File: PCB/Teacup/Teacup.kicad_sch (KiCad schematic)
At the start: 1 part

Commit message: pcb: pow + clock + usb
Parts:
- added C? (x2): TBD, Capacitor_SMD:C_0402_1005Metric, symbol Device:C
- added D?: D_TVS_Dual_AAC, symbol Device:D_TVS_Dual_AAC
- added J?: USB_C_Receptacle_USB2.0, symbol Connector:USB_C_Receptacle_USB2.0
- added R0, R1: 100k, Resistor_SMD:R_0603_1608Metric_Pad0.98x0.95mm_HandSolder, symbol Device:R
- added R? (x2): 5k1, Resistor_SMD:R_0603_1608Metric_Pad0.98x0.95mm_HandSolder, symbol Device:R
- added Y?: 24 MHz, Crystal:Crystal_SMD_2016-4Pin_2.0x1.6mm, symbol Device:Crystal_GND24
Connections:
- net +0V8: now also 1.10 (VDD_1), 1.30 (MIPI_AVD08), 1.39 (VDD_2), 1.55 (VDD_3), 1.72 (VDD_4), 1.78 (DDRPLL_VCCD), 1.83 (VDD_5)
- net +1V8: now also 1.3 (VDDIO_OSC), 1.31 (MIPI_AVD18), 1.33 (ADC_VREF), 1.34 (ADC_AVDD), 1.38 (USB_AVD18), 1.43 (CODEC_AVDD), 1.6 (PLL_VDDHV), 1.75 (DDRVDD), 1.76 (VDDMEM), 1.77 (VREF), 1.79 (DDRPLL_VCCA), 1.9 (VDDIO0)
- net +3V3: now also 1.37 (USB_AVD33), 1.40 (VDDIO2), 1.56 (VDDIO1_1), 1.84 (VDDIO1_2), R1.1
- net +5V: now also J?.A4 (VBUS), J?.A9 (VBUS), J?.B4 (VBUS), J?.B9 (VBUS)
- net GND: now also 1.8 (EFUSE_AVD), 1.89 (EP), C?.1, C?.2, D?.3 (common), J?.A1 (GND), J?.A12 (GND), J?.B1 (GND), J?.B12 (GND), R0.1, R?.1, R?.1, Y?.2, Y?.4
- net USB_D-: now reaches 1.35 (USB0PN)
- net USB_D-: now also D?.1 (A1), J?.A7 (D-), J?.B7 (D-)
- net USB_D+: now reaches 1.36 (USB0PP)
- net USB_D+: now also D?.2 (A2), J?.A6 (D+), J?.B6 (D+)
- net at 1.4 (EXCLK_O): now also C?.1, Y?.3
- net at 1.5 (EXCLK_I): now also C?.2, Y?.1
- net at 1.67 (BOOT_SEL0_PC00): now also R0.2, R1.2
- new net: J?.A5 (CC1), R?.2
- new net: J?.B5 (CC2), R?.2
- no-connect marks 0 -> 4
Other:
- note added: "Boot Selection R1 - NOR - MMC - USB R0 - MMC - USB"
- note added: "General purpose I/O: 1.5~3.6V DDR I/O: 1.8V(DDR2) ± 0.1V EFUSE programming: 1.8V ± 10% Analog power supply 1: 1.8V ± 10% Analog power supply 2: 3.3V ± 10% Core: 0.8V ± 0.1V 9 VDDIO0: IO digital power for DVP power domain, 1.8V 56,84 VDDIO1: IO digital power for normal function Pad power domain,1.8V/3.3V 40 VDDIO2: IO digital power for normal function Pad power domain, 1.8V/3.3V 10,39,55,72,83 VDD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"

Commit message: pcb: regulators
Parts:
- added C? (x6): 10uF, Capacitor_SMD:C_0402_1005Metric, symbol Device:C
- added C? (x6): 100nF, Capacitor_SMD:C_0402_1005Metric, symbol Device:C
- added C? (x6): 1uF, Capacitor_SMD:C_0402_1005Metric, symbol Device:C
- added R? (x6): 0R, Resistor_SMD:R_0603_1608Metric_Pad0.98x0.95mm_HandSolder, symbol Device:R
- added U?: AZ1117-1.8, symbol Regulator_Linear:AZ1117-1.8
- added U?: AZ1117-3.3, symbol Regulator_Linear:AZ1117-3.3
- added U?: MCP1826S, symbol Regulator_Linear:MCP1826S
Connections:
- net +0V8: now also R?.1
- net +1V8: now also R?.1
- net +3V3: now also R?.1, R?.1, R?.1
- net +5V: now also R?.1
- net GND: now also C?.2, C?.2, C?.2, C?.2, C?.2, C?.2, C?.2, C?.2, C?.2, C?.2, C?.2, C?.2, C?.2, C?.2, C?.2, C?.2, C?.2, C?.2, U?.1 (GND), U?.1 (GND), U?.2 (GND)
- new net: C?.1, C?.1, C?.1, R?.2, U?.3 (VI) (x2)
- new net: C?.1, C?.1, C?.1, R?.2, U?.2 (VO) (x2)
- new net: C?.1, C?.1, C?.1, R?.2, U?.1 (VI)
- new net: C?.1, C?.1, C?.1, R?.2, U?.3 (VO)
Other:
- moved on the sheet: 1, C?, D?, J?, R0, R1, R?, Y?

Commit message: pcb: flash + footprints
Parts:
- added C19, C23, C24: 100nF, Capacitor_SMD:C_0603_1608Metric_Pad1.08x0.95mm_HandSolder, symbol Device:C
- added C22: 4.7uF, Capacitor_SMD:C_0603_1608Metric_Pad1.08x0.95mm_HandSolder, symbol Device:C
- added J2: SD_Card, symbol Connector:SD_Card
- added R10, R11, R12, R13, R14: 100k, Resistor_SMD:R_0603_1608Metric_Pad0.98x0.95mm_HandSolder, symbol Device:R
- added R15, R16, R17, R18, R19, R20: 47k, Resistor_SMD:R_0603_1608Metric_Pad0.98x0.95mm_HandSolder, symbol Device:R
- added R21: 1M, Resistor_SMD:R_0402_1005Metric, symbol Device:R
- added U4: W25Q32JVSS, Package_SO:SOIC-8_5.23x5.23mm_P1.27mm, symbol Memory_Flash:W25Q32JVSS
- C1, C10, C11, C12, C13, C14, C15, C16, C17, C18, C2, C3, C4, C5, C6, C7, C8, C9: renamed from C?; footprint Capacitor_SMD:C_0402_1005Metric -> Capacitor_SMD:C_0603_1608Metric_Pad1.08x0.95mm_HandSolder
- D1: renamed from D?; footprint (none) -> Package_TO_SOT_SMD:SOT-323_SC-70
- IC1: renamed from 1; Reference_1 IC -> (none); Value_1 T31ZX -> (none)
- gave numbers to parts that had none: 15
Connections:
- net +1V8: now also R10.1; no longer IC1.77 (VREF)
- net +3V3: now also C23.1, C24.1, J2.4 (VDD), R12.2, R13.1, R14.2, R15.1, R16.1, R17.1, R18.1, R19.1, R20.1, U4.8 (VCC)
- net GND: now also C19.1, C22.2, C23.2, C24.2, J2.3 (VSS), J2.6 (VSS), R11.1, U4.4 (GND)
- net at C21.1, IC1.4 (EXCLK_O), Y1.3: now also R21.2
- net at IC1.42 (VCM): now also C22.1
- net NOR_CE: now reaches IC1.45 (SFC_CE0_PA28)
- net NOR_CE: now also R12.1, U4.1 (~{CS})
- net NOR_DR: now reaches IC1.46 (SFC_DR_PA24)
- net NOR_DR: now also U4.2 (DO(IO1))
- net NOR_DT: now reaches IC1.47 (SFC_DT_PA23)
- net NOR_DT: now also U4.5 (DI(IO0))
- net NOR_CK: now reaches IC1.48 (SFC_CLK_PA27)
- net NOR_CK: now also U4.6 (CLK)
- net MMC0_D1: now reaches IC1.49 (MSC0_D1_SSI_SLV_DR_PB01)
- net MMC0_D1: now also J2.8 (DAT1), R20.2
- net at C20.2, IC1.5 (EXCLK_I), Y1.1: now also R21.1
- net MMC0_D0: now reaches IC1.50 (MSC0_D0_SSI_SLV_DT_PB00)
- net MMC0_D0: now also J2.7 (DAT0), R19.2
- net MMC0_CLK: now reaches IC1.51 (MSC0_CLK_SSI_SLV_CLK_PB04)
- net MMC0_CLK: now also J2.5 (CLK), R18.2
- net MMC0_CMD: now reaches IC1.52 (MSC0_CMD_SSI_SLV_CE0_PB05)
- net MMC0_CMD: now also J2.2 (CMD), R17.2
- net MMC0_D3: now reaches IC1.53 (MSC0_D3_PB03)
- net MMC0_D3: now also J2.1 (CD/DAT3), R16.2
- net MMC0_D2: now reaches IC1.54 (MSC0_D2_PB02)
- net MMC0_D2: now also J2.9 (DAT2), R15.2
- new net: R13.2, U4.3 (IO2)
- new net: C19.2, IC1.77 (VREF), R10.2, R11.2
- new net: R14.1, U4.7 (IO3)
- no-connect marks 4 -> 8
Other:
- note added: "General purpose I/O: 1.5~3.6V DDR I/O: 1.8V(DDR2) ± 0.1V EFUSE programming: 1.8V ± 10% Analog power supply 1: 1.8V ± 10% Analog power supply 2: 3.3V ± 10% Core: 0.8V ± 0.1V"
- note removed: "General purpose I/O: 1.5~3.6V DDR I/O: 1.8V(DDR2) ± 0.1V EFUSE programming: 1.8V ± 10% Analog power supply 1: 1.8V ± 10% Analog power supply 2: 3.3V ± 10% Core: 0.8V ± 0.1V 9 VDDIO0: IO digital power for DVP power domain, 1.8V 56,84 VDDIO1: IO digital power for normal function Pad power domain,1.8V/3.3V 40 VDDIO2: IO digital power for normal function Pad power domain, 1.8V/3.3V 10,39,55,72,83 VDD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"
- moved on the sheet: C20, C21, Y1

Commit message: pcb: sch done, initial placement
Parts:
- added J3: SFW15R-2STE1LF, Footprints:SFW15R2STE1LF, symbol SFW15R-2STE1LF:SFW15R-2STE1LF
- added J4: EXP0, Connector_PinHeader_2.54mm:PinHeader_1x10_P2.54mm_Vertical, symbol Connector:Conn_01x10_Female
- added J5: UART, Connector_PinHeader_2.54mm:PinHeader_1x03_P2.54mm_Vertical, symbol Connector:Conn_01x03_Female
- added J6: EXP2, Connector_PinHeader_2.54mm:PinHeader_1x16_P2.54mm_Vertical, symbol Connector:Conn_01x16_Female
- added J7: EXP1, Connector_PinHeader_2.54mm:PinHeader_1x16_P2.54mm_Vertical, symbol Connector:Conn_01x16_Female
- J1: footprint (none) -> Connector_USB:USB_C_Receptacle_HRO_TYPE-C-31-M-12
- J2: footprint (none) -> Connector_Card:SD_Hirose_DM1AA_SF_PEJ82
- U1, U2, U3: footprint (none) -> Kicad:SOT-223-3_TabPin2
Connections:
- net +3V3: now also J3.15, J6.15 (Pin_15), J6.16 (Pin_16)
- net GND: now also J3.1, J3.10, J3.4, J3.7, J5.3 (Pin_3), J6.1 (Pin_1), J6.11 (Pin_11), J6.14 (Pin_14), J6.5 (Pin_5), J6.8 (Pin_8)
- net at IC1.1 (PWM0_SSI1_DT_PB17): now also J7.15 (Pin_15)
- net CAM_PE: now reaches IC1.11 (SA2_PA18)
- net CAM_PE: now also J3.11
- net I2C0_SCK: now reaches IC1.12 (SD7_SMB0_SCK_PA13)
- net I2C0_SCK: now also J3.13
- net I2C0_SDA: now reaches IC1.13 (SD6_SMB0_SDA_PA12)
- net I2C0_SDA: now also J3.14
- net PA17: now reaches IC1.14 (RD_DVP_VSYNC_SMB1_SCK_MSC1_CMD_PA17)
- net PA17: now also J4.10 (Pin_10)
- net PA16: now reaches IC1.15 (CS2_DVP_HSYNC_SMB1_SDA_MSC1_CLK_PA16)
- net PA16: now also J4.9 (Pin_9)
- net PA15: now reaches IC1.16 (SA1_DVP_MCLK_PA15)
- net PA15: now also J4.8 (Pin_8)
- net PA14: now reaches IC1.17 (SA0_DVP_PCLK_PWM0_PA14)
- net PA14: now also J4.7 (Pin_7)
- net PA11: now reaches IC1.18 (SD5_DVP_D11_UART2_RXD_MSC1_D3_PA11)
- net PA11: now also J4.6 (Pin_6)
- net PA10: now reaches IC1.19 (SD4_DVP_D10_UART2_TXD_MSC1_D2_PA10)
- net PA10: now also J4.5 (Pin_5)
- net at IC1.2 (PWM1_SSI1_DR_PB18): now also J7.16 (Pin_16)
- net PA09: now reaches IC1.20 (SD3_DVP_D9_UART2_RTS_MSC1_D1_PA09)
- net PA09: now also J4.4 (Pin_4)
- net PA08: now reaches IC1.21 (SD2_DVP_D8_UART2_CTS_MSC1_D0_PA08)
- net PA08: now also J4.3 (Pin_3)
- net PA07: now reaches IC1.22 (SD1_DVP_D7_UART1_RXD_PA07)
- net PA07: now also J4.2 (Pin_2)
- net PA06: now reaches IC1.23 (SD0_DVP6_UART1_TXD_PA06)
- net PA06: now also J4.1 (Pin_1)
- net MIPI_0_N: now reaches IC1.24 (MIPI_DATAN0_DVP_D5)
- net MIPI_0_N: now also J3.2
- net MIPI_0_P: now reaches IC1.25 (MIPI_DATAP0_DVP_D4)
- net MIPI_0_P: now also J3.3
- net MIPI_CLK_N: now reaches IC1.26 (MIPI_CLKN_DVP_D3)
- net MIPI_CLK_N: now also J3.8
- net MIPI_CLK_P: now reaches IC1.27 (MIPI_CLKP_DVP_D2)
- net MIPI_CLK_P: now also J3.9
- net MIPI_1_N: now reaches IC1.28 (MIPI_DATAN1_DVP_D1)
- net MIPI_1_N: now also J3.5
- net MIPI_1_P: now reaches IC1.29 (MIPI_DATAP1_DVP_D0)
- net MIPI_1_P: now also J3.6
- net AUX0: now reaches IC1.32 (ADC_AUX0)
- net AUX0: now also J6.2 (Pin_2)
- net MICLP: now reaches IC1.41 (MICLP)
- net MICLP: now also J6.3 (Pin_3)
- net HPOUTL: now reaches IC1.44 (HPOUTL)
- net HPOUTL: now also J6.4 (Pin_4)
- net at IC1.57 (GMAC_MDIO_MSC1_D1_SLCD_D5_PB11): now also J7.1 (Pin_1)
- net at IC1.58 (GMAC_MDCK_MSC1_D0_I2S_SDTO_SLCD_D4_PB10): now also J7.2 (Pin_2)
- net at IC1.59 (GMAC_RXDV_MSC1_CMD_I2S_SDTI_SLCD_D3_PB09): now also J7.3 (Pin_3)
- net at IC1.60 (GMAC_RXD0_I2S_DAC_LRCK_SLCD_WR_PB15/_SFC_CE1_PA26): now also J7.4 (Pin_4)
- net at IC1.61 (GMAC_RXD1_SLCD_TE_PB16/_SFC_GPC_PA25): now also J7.5 (Pin_5)
- net at IC1.62 (GMAC_TXCLK_SLCD_D0_PB06): now also J7.6 (Pin_6)
- net at IC1.63 (GMAC_PHY_CLK_SLCD_D1_PB07): now also J7.7 (Pin_7)
- net at IC1.64 (GMAC_TXD0_MSC1_D2_I2S_ADC_LRCK_SLCD_D6_PB13): now also J7.8 (Pin_8)
- net at IC1.65 (GMAC_TXD1_MSC1_D3_I2S_DAC_MCLK_SLCD_D7_PB14): now also J7.9 (Pin_9)
- net at IC1.66 (GMAC_TXEN_MSC1_CLK_I2S_ADC_MCLK_SLCD_D2_PB08): now also J7.10 (Pin_10)
- net at IC1.68 (UART0_RTS_I2S_DAC_BCLK_SLCD_DC_PB21): now also J7.11 (Pin_11)
- net at IC1.69 (UART0_CTS_I2S_ADC_BCLK_SLCD_CS_PB20): now also J7.12 (Pin_12)
- net at IC1.70 (UART0_TXD_TDO_SLCD_RDY_PB22): now also J7.13 (Pin_13)
- net at IC1.71 (UART0_RXD_TDI_PB19): now also J7.14 (Pin_14)
- net UART_RX: now reaches IC1.73 (UART1_RXD_TMS_PB24)
- net UART_RX: now also J5.2 (Pin_2)
- net UART_TX: now reaches IC1.74 (UART1_TXD_TCK_PB23)
- net UART_TX: now also J5.1 (Pin_1)
- net CAM_LED: now reaches IC1.80 (GPIO_PB31)
- net CAM_LED: now also J3.12
- net PB30: now reaches IC1.81 (SSI1_CE0_DMIC_DAT1_PB30)
- net PB30: now also J6.13 (Pin_13)
- net PB29: now reaches IC1.82 (SSI1_CLK_DMIC_DAT0_PB29)
- net PB29: now also J6.12 (Pin_12)
- net PB28: now reaches IC1.85 (PWM3_SSI1_DR_DMIC_CLK_PB28)
- net PB28: now also J6.10 (Pin_10)
- net PB27: now reaches IC1.86 (PWM2_SSI1_DT_DRV_VBUS_PB27)
- net PB27: now also J6.9 (Pin_9)
- net PB26: now reaches IC1.87 (SMB1_SCK_SSI1_CLK_PB26)
- net PB26: now also J6.7 (Pin_7)
- net PB25: now reaches IC1.88 (SMB1_SDA_SSI1_CE0_PB25)
- net PB25: now also J6.6 (Pin_6)
- no-connect marks 8 -> 10

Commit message: pcb: routed high speed signals
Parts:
- added C25, C26, C28, C30, C31, C32, C34, C35, C36, C37, C38, C39, C40, C41, C42, C43, C44, C45, C46: 100nF, Capacitor_SMD:C_0402_1005Metric, symbol Device:C
- added TP1, TP2, TP3, TP4, TP5, TP6, TP7, TP8, TP9: TestPoint, TestPoint:TestPoint_Pad_D1.5mm, symbol Connector:TestPoint
- added U5: W25Q32JVSS, Package_DIP:DIP-8_W7.62mm_Socket_LongPads, symbol Memory_Flash:W25Q32JVSS
- C23, C24: footprint Capacitor_SMD:C_0603_1608Metric_Pad1.08x0.95mm_HandSolder -> Capacitor_SMD:C_0402_1005Metric
- J1: value USB_C_Receptacle_USB2.0 -> USB Type-C; Manufacturer (none) -> Korean Hroparts Elec; Manufacturer Part Number (none) -> TYPE-C-31-M-12
- J4, J5, J6, J7: now left out of the parts list
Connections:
- net +0V8: now also C37.1, C41.1, C42.1, C43.1, C44.1, C45.1, C46.1
- net +1V8: now also C25.1, C26.1, C28.1, C30.1, C31.1, C32.1, C34.1, C35.1
- net +3V3: now also C36.1, C38.1, C39.1, C40.1, U5.8 (VCC)
- net GND: now also C25.2, C26.2, C28.2, C30.2, C31.2, C32.2, C34.2, C35.2, C36.2, C37.2, C38.2, C39.2, C40.2, C41.2, C42.2, C43.2, C44.2, C45.2, C46.2, TP8.1, U5.4 (GND)
- net I2C0_SCK: now also TP9.1
- net I2C0_SDA: now also TP7.1
- net NOR_CE: now also U5.1 (~{CS})
- net NOR_CK: now also U5.6 (CLK)
- net NOR_DR: now also U5.2 (DO(IO1))
- net NOR_DT: now also U5.5 (DI(IO0))
- net USB_D+: now also TP5.1
- net USB_D-: now also TP3.1
- net at R13.2, U4.3 (IO2): now also U5.3 (IO2)
- net at C4.1, C5.1, C6.1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: now also TP2.1
- net at C16.1, C17.1, C18.1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: now also TP6.1
- net at C10.1, C11.1, C12.1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: now also TP4.1
- net at C1.1, C2.1, C3.1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: now also TP1.1
- net at R14.1, U4.7 (IO3): now also U5.7 (IO3)
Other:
- note added: "Flash Socket"
- moved on the sheet: C23, C24, J2, R12, R13, R14, R15, R16, R17, R18, R19, R20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

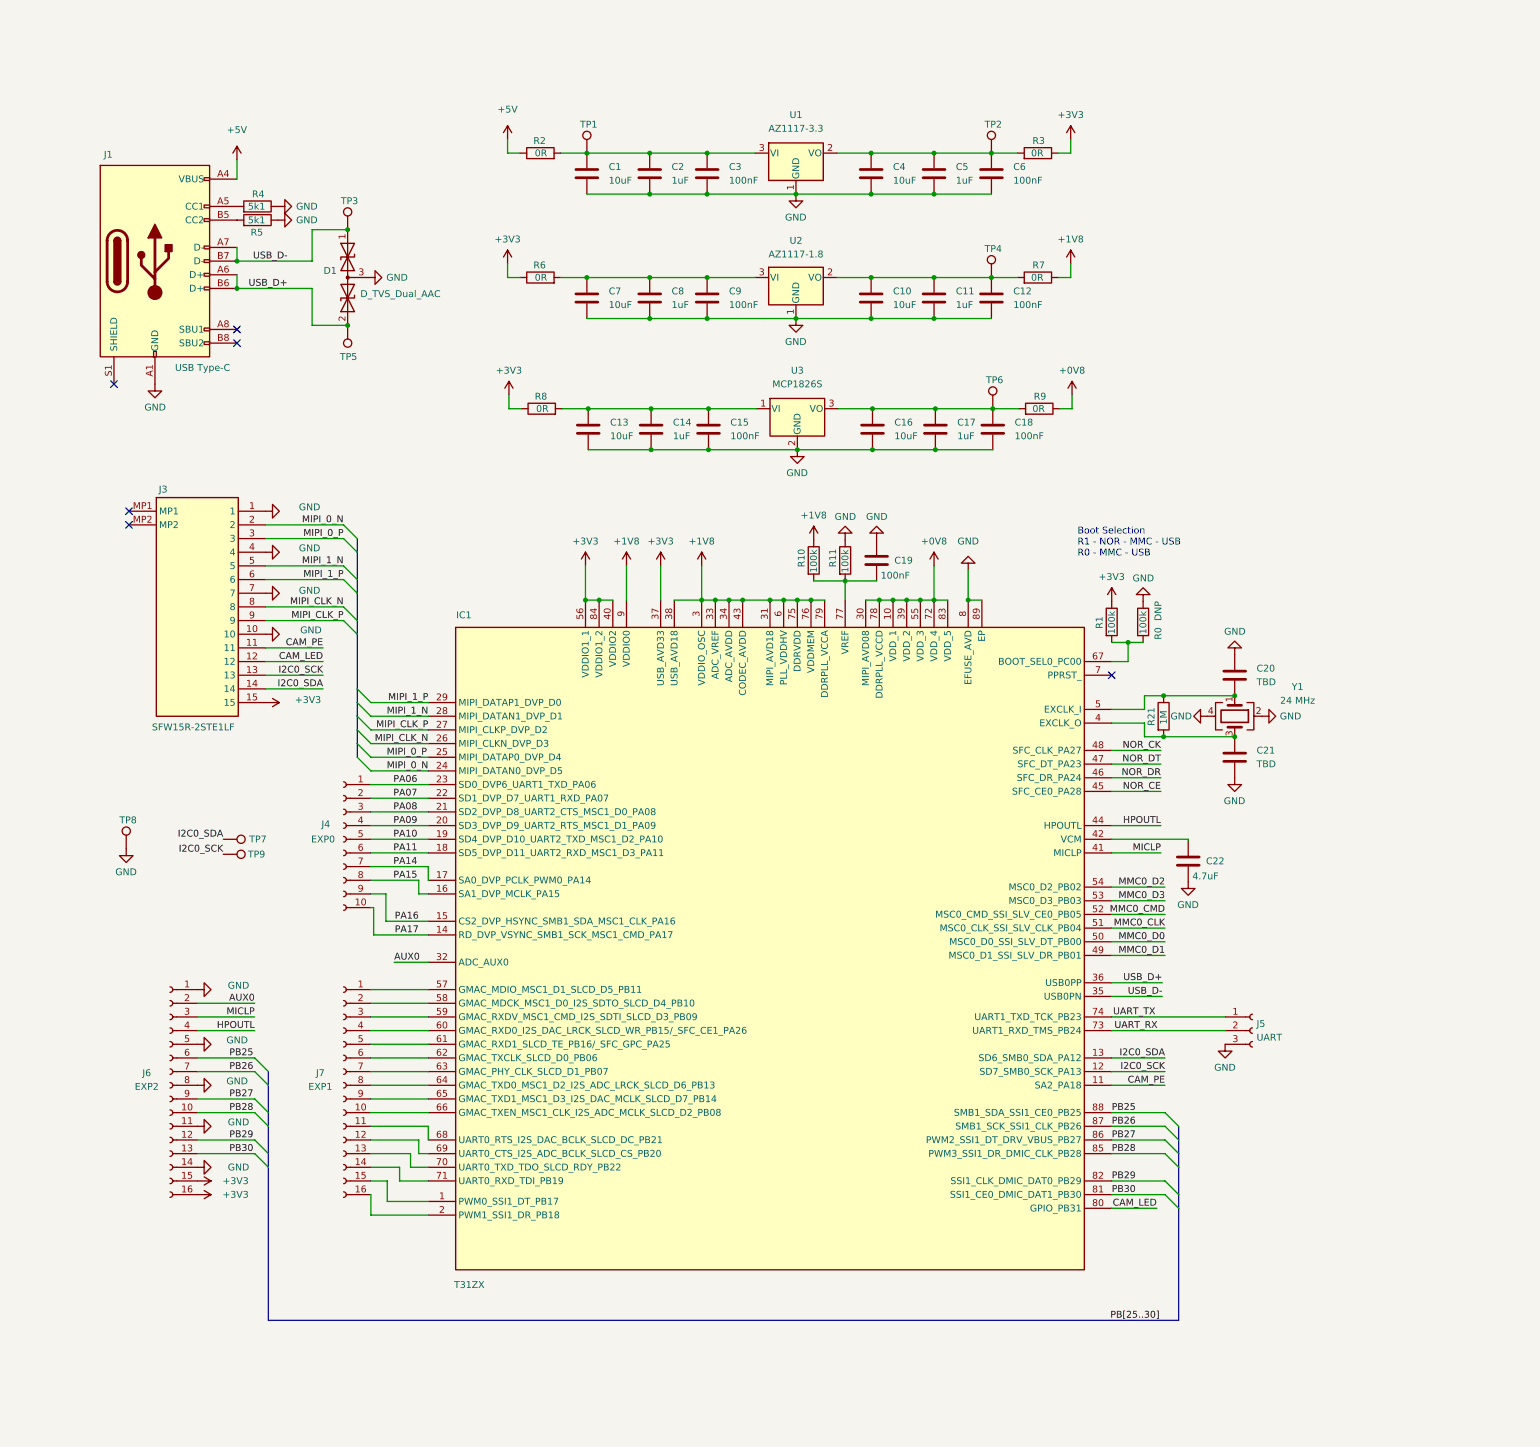
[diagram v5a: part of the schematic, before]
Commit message: pcb: routing done
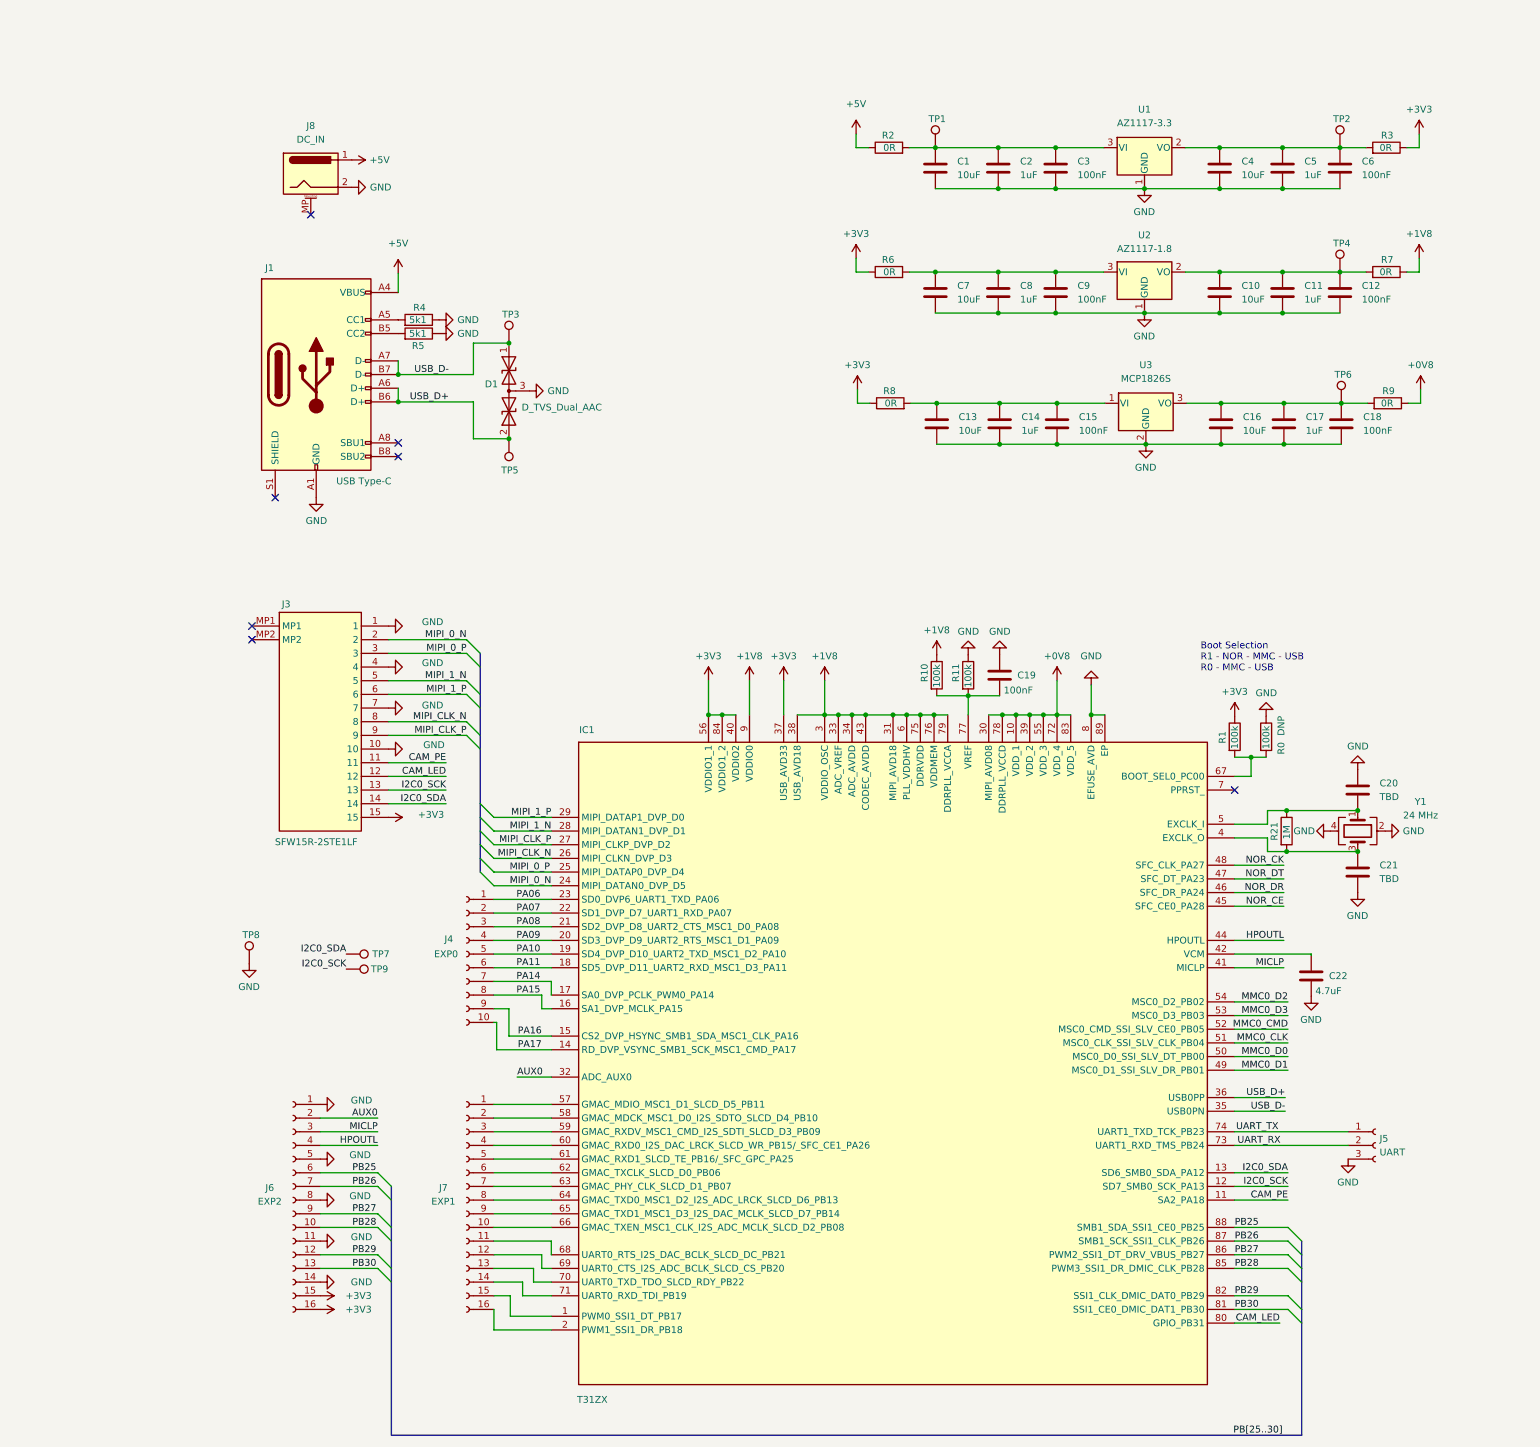
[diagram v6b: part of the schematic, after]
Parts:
- added J8: DC_IN, symbol Connector:Barrel_Jack_MountingPin
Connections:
- net +5V: now also J8.1
- net GND: now also J8.2
- no-connect marks 10 -> 11
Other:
- moved on the sheet: C1, C10, C11, C12, C13, C14, C15, C16, C17, C18, C19, C2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
